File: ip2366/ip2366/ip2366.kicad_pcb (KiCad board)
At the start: 4 copper layers, 80 x 32 mm, 61 parts, among them CN1 XT30PW-M, Q1 RU3030M2-VB, SW1 K2-1112SW-A4SW-04, U1 IP2366 (I2C VERSION)

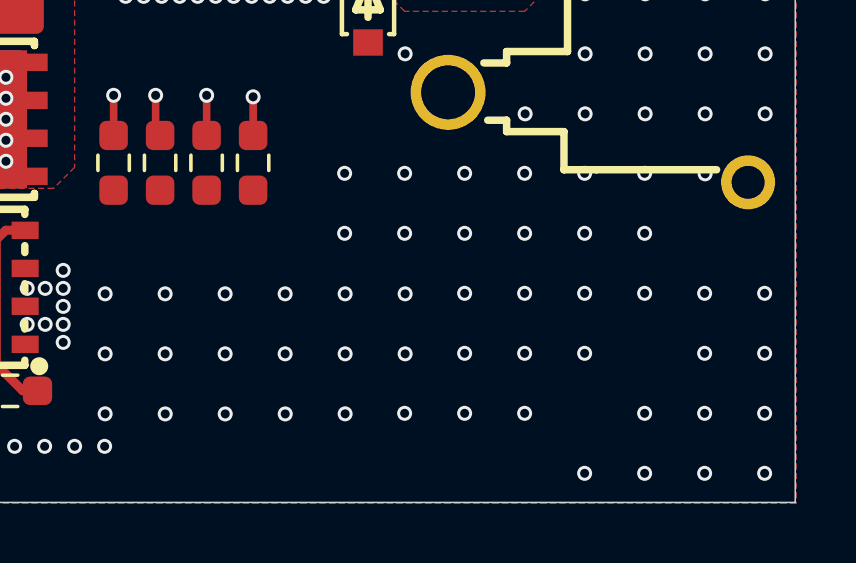
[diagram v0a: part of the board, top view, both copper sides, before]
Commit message: add logo
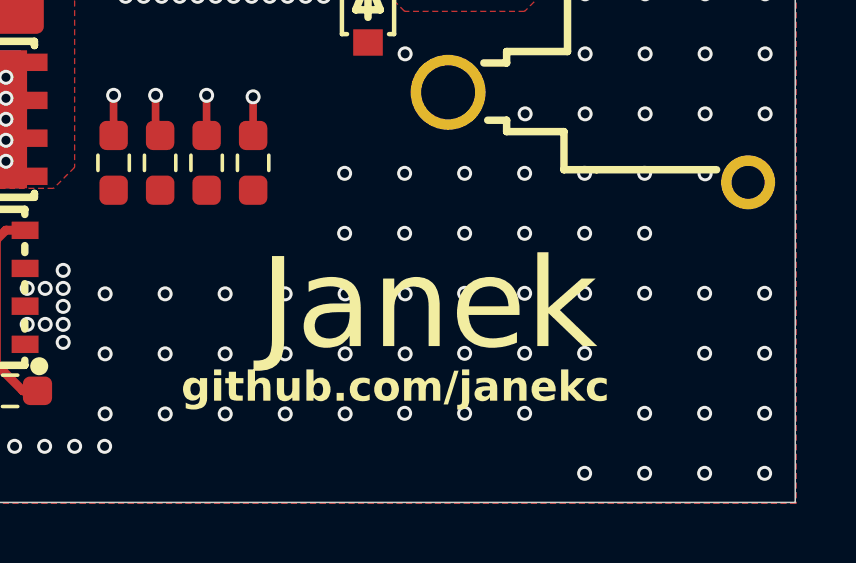
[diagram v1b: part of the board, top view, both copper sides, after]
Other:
- board text added: "Janek"
- board text added: "github.com/janekc"
